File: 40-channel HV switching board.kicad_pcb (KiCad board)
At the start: 4 copper layers, 84 x 94 mm, 194 parts, among them IC1 ATMEGA328P-A, J1 TFM-125-02-X-DH, P1 CONN_01X06, P2 CONN_01X06, P3 CONN_01X01, P4 CONN_01X01, P5 CONN_01X01, P6 CONN_01X01, U1 74HC595A, U2 74HC595A, U3 74HC595A, U4 74HC595A, U5 74HC595A, U6 W25Q64FV, Y1 RESONATOR

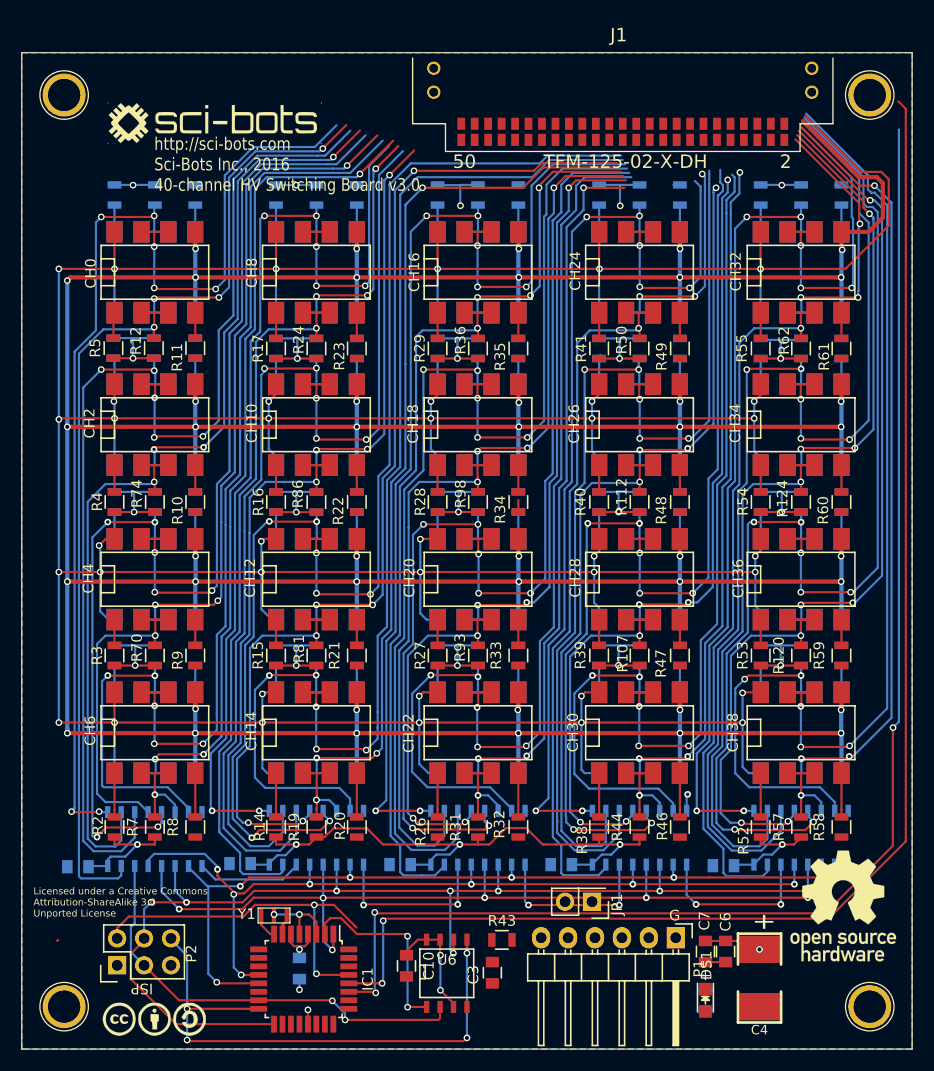
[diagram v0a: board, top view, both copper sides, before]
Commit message: Lots of fixes to prepare for EMC testing
* read output of shift registers
* fix flash chip connection
* replace jumpers with 0805 pads
* reduce length to 92mm
* filter i2c lines
* protect i2c lines
* add ferrites to SPI lines
* add chasis ground ring
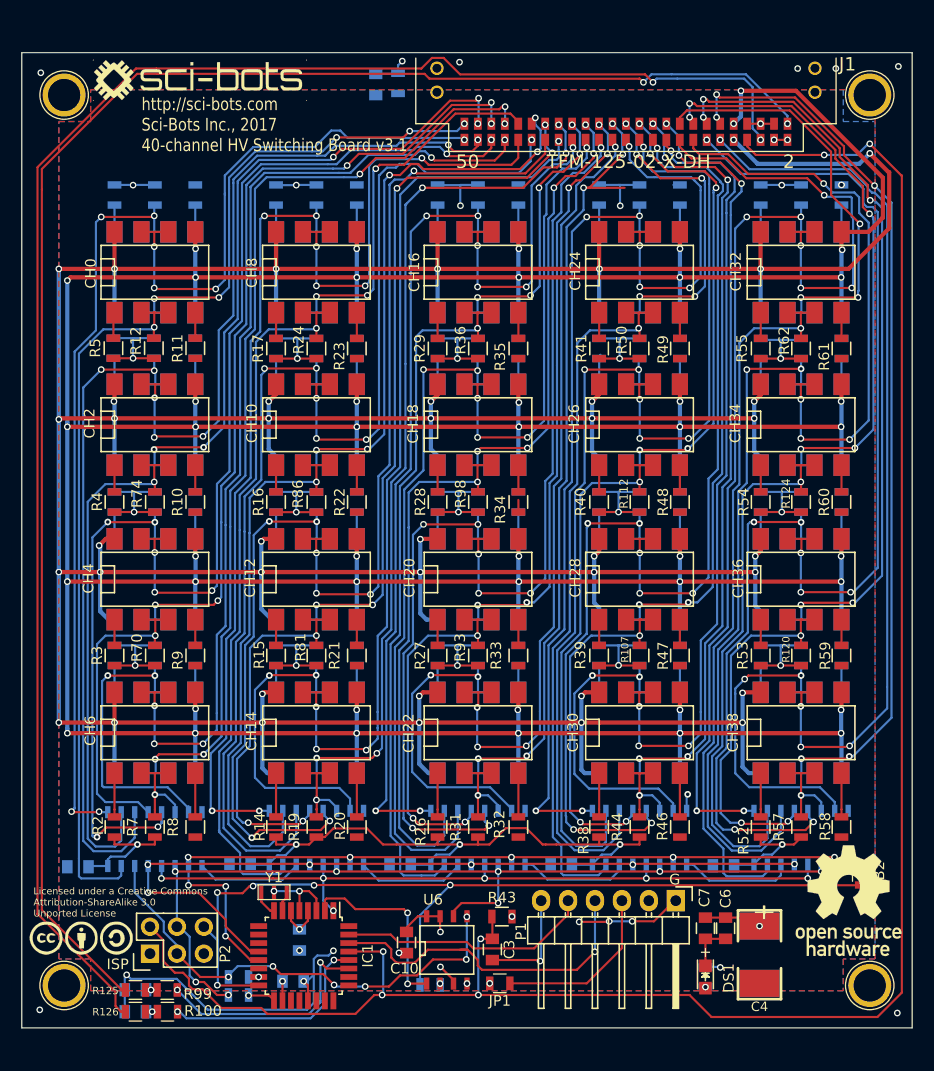
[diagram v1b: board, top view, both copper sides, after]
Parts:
- added C11: 0.1uF, Capacitors_SMD:C_0805, B.Cu at (49.6, 110.6)
- added C14: C, Capacitors_SMD:C_0805, B.Cu at (34.7, 111.4)
- added C15: C, Capacitors_SMD:C_0805, B.Cu at (34.7, 113.5)
- added C16: 0.1uF, Capacitors_SMD:C_0805, B.Cu at (57.4, 26.0)
- added FB1: FERRITE, Resistors_SMD:R_0805, B.Cu at (44.5, 110.2)
- added FB2: FERRITE, Resistors_SMD:R_0805, F.Cu at (103.2, 100.6)
- added FB3: FERRITE, Resistors_SMD:R_0805, B.Cu at (44.5, 111.9)
- added FB4: FERRITE, Resistors_SMD:R_0805, B.Cu at (62.5, 111.0)
- added FB5: FERRITE, Resistors_SMD:R_0805, B.Cu at (59.5, 25.9)
- added R100: R, Resistors_SMD:R_0805, F.Cu at (37.8, 113.5)
- added R125: R, Resistors_SMD:R_0805, F.Cu at (34.7, 111.4)
- added R126: R, Resistors_SMD:R_0805, F.Cu at (34.7, 113.5)
- added R99: R, Resistors_SMD:R_0805, F.Cu at (37.7, 111.4)
- JP1: footprint Pin_Headers:Pin_Header_Straight_2x01 -> Resistors_SMD:R_0805
- moved JP1 11.6 mm to (69.1, 110.8)
- moved G*** 10.3 mm to (29.6, 106.5)
- moved G*** 4.29 mm to (40.8, 25.6)
- moved P1 3.50 mm to (85.7, 103.0)
- moved P2 3.29 mm to (36.1, 108.0)
- moved C13 2.70 mm to (50.2, 106.7)
- moved C10 2.20 mm to (60.3, 107.0)
- moved C2 2.20 mm to (93.6, 108.1)
- moved C3 2.20 mm to (68.4, 107.6)
- moved C4 2.20 mm to (93.6, 108.1)
- moved C6 2.20 mm to (90.4, 105.6)
- moved C7 2.20 mm to (88.5, 105.6)
- moved DS1 2.20 mm to (88.5, 110.2)
- moved IC1 2.20 mm to (50.6, 108.2)
- moved R43 2.20 mm to (69.3, 104.5)
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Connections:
- IC1 pad 15: D11/MOSI -> Net-(FB1-Pad1)
- IC1 pad 17: D13/SCK -> Net-(FB3-Pad1)
- IC1 pad 27: A4/SDA -> Net-(IC1-Pad27)
- IC1 pad 28: A5/SCL -> Net-(IC1-Pad28)
- J1 pad 1: HVOUT0 -> A4/SDA
- J1 pad 10: HVOUT9 -> HVGND
- J1 pad 11: HVOUT10 -> HVOUT39
- J1 pad 12: HVOUT11 -> HVOUT38
- J1 pad 13: HVOUT12 -> HVOUT37
- J1 pad 14: HVOUT13 -> HVOUT36
- J1 pad 15: HVOUT14 -> HVOUT35
- J1 pad 16: HVOUT15 -> HVOUT34
- J1 pad 17: HVOUT16 -> HVOUT33
- J1 pad 18: HVOUT17 -> HVOUT32
- J1 pad 19: HVOUT18 -> HVOUT31
- J1 pad 2: HVOUT1 -> +3.3V
- J1 pad 20: HVOUT19 -> HVOUT30
- J1 pad 21: HVOUT20 -> HVOUT29
- J1 pad 22: HVOUT21 -> HVOUT28
- J1 pad 23: HVOUT22 -> HVOUT27
- J1 pad 24: HVOUT23 -> HVOUT26
- J1 pad 25: HVOUT24 -> HVOUT25
- J1 pad 26: HVOUT25 -> HVOUT24
- J1 pad 27: HVOUT26 -> HVOUT23
- J1 pad 28: HVOUT27 -> HVOUT22
- J1 pad 29: HVOUT28 -> HVOUT21
- J1 pad 3: HVOUT2 -> GND
- J1 pad 30: HVOUT29 -> HVOUT20
- J1 pad 31: HVOUT30 -> HVOUT19
- J1 pad 32: HVOUT31 -> HVOUT18
- J1 pad 33: HVOUT32 -> HVOUT17
- J1 pad 34: HVOUT33 -> HVOUT16
- J1 pad 35: HVOUT34 -> HVOUT15
- J1 pad 36: HVOUT35 -> HVOUT14
- J1 pad 37: HVOUT36 -> HVOUT13
- J1 pad 38: HVOUT37 -> HVOUT12
- J1 pad 39: HVOUT38 -> HVOUT11
- J1 pad 4: HVOUT3 -> +3.3V
- J1 pad 40: HVOUT39 -> HVOUT10
- J1 pad 41: HV -> HVOUT9
- J1 pad 42: HVGND -> HVOUT8
- J1 pad 43: GND -> HVOUT7
- J1 pad 44: RST -> HVOUT6
- J1 pad 45: GND -> HVOUT5
- J1 pad 46: A5/SCL -> HVOUT4
- J1 pad 47: GND -> HVOUT3
- J1 pad 48: +3.3V -> HVOUT2
- J1 pad 49: A4/SDA -> HVOUT1
- J1 pad 5: HVOUT4 -> GND
- J1 pad 50: +3.3V -> HVOUT0
- J1 pad 6: HVOUT5 -> A5/SCL
- J1 pad 7: HVOUT6 -> GND
- J1 pad 8: HVOUT7 -> RST
- J1 pad 9: HVOUT8 -> HV
- P3 pad 1: GND -> CHASIS_GND
- P4 pad 1: GND -> CHASIS_GND
- P5 pad 1: GND -> CHASIS_GND
- P6 pad 1: GND -> CHASIS_GND
- U6 pad 2: D11/MOSI -> Net-(FB4-Pad1)
- U6 pad 5: D12/MISO -> D11/MOSI
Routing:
- net RST: track 35.0 -> 189.2 mm, vias 2 -> 6
- net GND: track 17.2 -> 62.8 mm, vias 5 -> 14
- net D12/MISO: track 53.0 -> 86.4 mm, vias 4 -> 5
- net TX: track 0.00 -> 32.3 mm, vias 0 -> 1
- net CHASIS_GND: track 0.00 -> 31.3 mm, vias 0 -> 8
- net A5/SCL: track 131.6 -> 161.9 mm
- net A4/SDA: track 129.6 -> 158.2 mm, vias 3 -> 2
- net RX: track 0.00 -> 23.9 mm
- net Net-(IC1-Pad27): track 0.00 -> 21.6 mm, vias 0 -> 2
- net Net-(IC1-Pad28): track 0.00 -> 20.7 mm, vias 0 -> 2
- net D13/SCK: track 108.2 -> 88.1 mm
- net HVOUT11: track 38.9 -> 55.6 mm, vias 3 -> 5
- net +3.3V_USB: track 0.00 -> 16.4 mm
- net HVOUT3: track 48.8 -> 64.1 mm, vias 3 -> 5
- net HVOUT35: track 42.4 -> 57.2 mm, vias 3 -> 5
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- added copper zone on GND, net CHASIS_GND
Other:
- board size 84 x 94 mm -> 84 x 92 mm
- board text added: "http://sci-bots.com Sci-Bots Inc., 2017 40-channel HV Switching Board v3.1"
- board text removed: "http://sci-bots.com Sci-Bots Inc., 2016 40-channel HV Switching Board v3.0"

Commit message: Update part numbers for i2c filters
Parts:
- C14, C15: value C -> 150pF
- R100, R99: value R -> 51
- R125, R126: value R -> 150
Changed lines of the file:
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@@
       (effects (font (size 0.8 0.8) (thickness 0.1)) (justify mirror))
     )
-    (fp_text value C (at 0 -1.75) (layer B.Fab)
+    (fp_text value 150pF (at 0 -1.75) (layer B.Fab)
       (effects (font (size 1 1) (thickness 0.15)) (justify mirror))
     )
@@
       (effects (font (size 0.8 0.8) (thickness 0.1)) (justify mirror))
     )
-    (fp_text value C (at 0 -1.75) (layer B.Fab)
+    (fp_text value 150pF (at 0 -1.75) (layer B.Fab)
       (effects (font (size 1 1) (thickness 0.15)) (justify mirror))
     )
@@
       (effects (font (size 1 1) (thickness 0.15)))
     )
-    (fp_text value R (at 0 1.75) (layer F.Fab)
+    (fp_text value 51 (at 0 1.75) (layer F.Fab)
       (effects (font (size 1 1) (thickness 0.15)))
     )
@@
       (effects (font (size 1 1) (thickness 0.15)))
     )
-    (fp_text value R (at 0 1.75) (layer F.Fab)
+    (fp_text value 51 (at 0 1.75) (layer F.Fab)
       (effects (font (size 1 1) (thickness 0.15)))
     )
@@
       (effects (font (size 0.7 0.7) (thickness 0.1)))
     )
-    (fp_text value R (at 0 1.75) (layer F.Fab)
+    (fp_text value 150 (at 0 1.75) (layer F.Fab)
       (effects (font (size 1 1) (thickness 0.15)))
     )
@@
       (effects (font (size 0.7 0.7) (thickness 0.1)))
     )
-    (fp_text value R (at 0 1.75) (layer F.Fab)
-      (effects (font (size 1 1) (thickness 0.15)))
-    )
+    (fp_text value 150 (at 0 1.75) (layer F.Fab)
+      (effects (font (size 1 1) (thickness 0.15)))
+    )

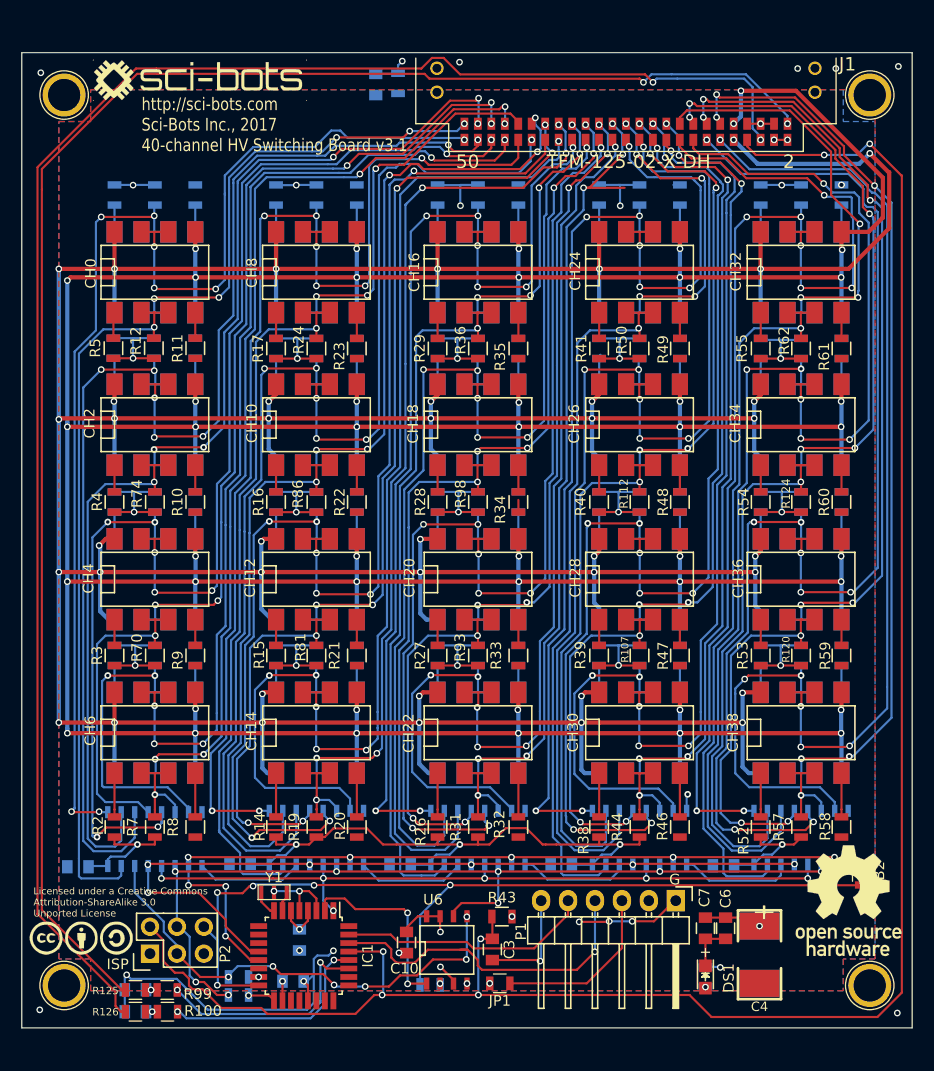
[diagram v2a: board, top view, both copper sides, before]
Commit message: Change resistor values use standard ref prefixes
* Fix #1 and #2
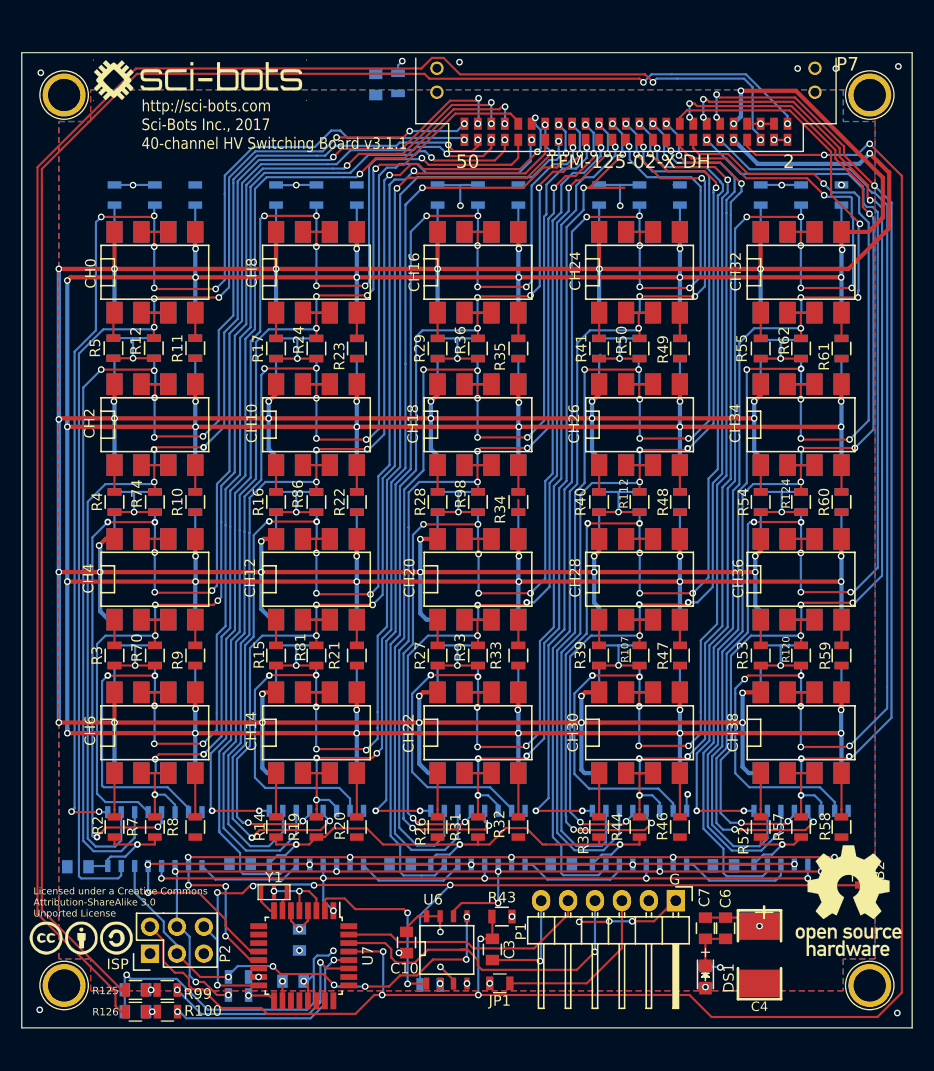
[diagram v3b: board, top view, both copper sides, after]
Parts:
- CH0, CH1, CH10, CH11, CH12, CH13, CH14, CH15, CH16, CH17, CH18, CH19, CH2, CH20, CH21, CH22, CH23, CH24, CH25, CH26, CH27, CH28, CH29, CH3, CH30, CH31, CH32, CH33, CH34, CH35, CH36, CH37, CH38, CH39, CH4, CH5, CH6, CH7, CH8, CH9: value AQW216 -> SSR-DPST
- R10, R102, R103, R104, R105, R108, R109, R11, R110, R111, R113, R115, R116, R117, R119, R121, R122, R123, R14, R15, R16, R17, R2, R20, R21, R22, R23, R26, R27, R28, R29, R3, R32, R33, R34, R35, R38, R39, R4, R40, R41, R46, R47, R48, R49, R5, R52, R53, R54, R55, R58, R59, R60, R61, R63, R65, R66, R67, R69, R71, R72, R73, R76, R77, R78, R79, R8, R82, R83, R84, R85, R88, R89, R9, R90, R91, R94, R95, R96, R97: value 300 -> 220
- U7: renamed from IC1; value ATMEGA328P-A -> ATMEGA328P-AU
- renumbered J1 to P7
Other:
- board text added: "http://sci-bots.com Sci-Bots Inc., 2017 40-channel HV Switching Board v3.1.1"
- board text removed: "http://sci-bots.com Sci-Bots Inc., 2017 40-channel HV Switching Board v3.1"

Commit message: Modify to use Sci-Bots library submodule
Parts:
- C2, C4: footprint WheelerLab:SM2917 -> Sci-Bots:SM2917
- G***: footprint WheelerLab:OSHW_logo_10mm -> Sci-Bots:OSHW_logo_10mm
- G***: footprint WheelerLab:CC_S_A_logo_10mm -> Sci-Bots:CC_S_A_logo_10mm
- P7: footprint WheelerLab:TFM-125-02-X-DH -> Sci-Bots:TFM-125-02-X-DH
- U1, U2, U3, U4, U5: footprint WheelerLab:SO16E -> Sci-Bots:SO16E
- Y1: footprint WheelerLab:CSTCE_G15C -> Sci-Bots:CSTCE_G15C
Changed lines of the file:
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@@
       (xy 10.0584 -1.9304) (xy 10.100851 -1.91244)) (layer F.SilkS) (width 0.01))
   )
-  (module WheelerLab:SM2917 (layer Back)
+  (module Sci-Bots:SM2917 (layer Back)
     (at 93.6 108.1 270)
     (fp_text reference C2 (at -3.5 -3.2 360) (layer B.SilkS)
@@
     )
   )
-  (module WheelerLab:SM2917 (layer Front)
+  (module Sci-Bots:SM2917 (layer Front)
     (at 93.6 108.1 270)
     (fp_text reference C4 (at 4.9 0 360) (layer F.SilkS)
@@
     )
   )
-  (module WheelerLab:SO16E (layer Back)
+  (module Sci-Bots:SO16E (layer Back)
     (at 36.56125 97.19175)
     (descr "Module CMS SOJ 16 pins etroit")
@@
     )
   )
-  (module WheelerLab:SO16E (layer Back)
+  (module Sci-Bots:SO16E (layer Back)
     (at 51.80125 97.06475)
     (descr "Module CMS SOJ 16 pins etroit")
@@
     )
   )
-  (module WheelerLab:SO16E (layer Back)
+  (module Sci-Bots:SO16E (layer Back)
     (at 67.04125 97.06475)
     (descr "Module CMS SOJ 16 pins etroit")
@@
     )
   )
-  (module WheelerLab:SO16E (layer Back)
+  (module Sci-Bots:SO16E (layer Back)
     (at 82.28125 97.06475)
     (descr "Module CMS SOJ 16 pins etroit")
@@
     )
   )
-  (module WheelerLab:SO16E (layer Back)
+  (module Sci-Bots:SO16E (layer Back)
     (at 97.52125 97.06475)
     (descr "Module CMS SOJ 16 pins etroit")
@@
     )
   )
-  (module WheelerLab:OSHW_logo_10mm (layer Front)
+  (module Sci-Bots:OSHW_logo_10mm (layer Front)
     (at 102 103)
     (fp_text reference G*** (at 0 0) (layer F.SilkS) hide
@@
       (xy -0.522042 -5.212843) (xy -0.507346 -5.226922) (xy 0.507808 -5.226922) (xy 0.522657 -5.211981)) (layer F.SilkS) (width 0.01))
   )
-  (module WheelerLab:CC_S_A_logo_10mm (layer Front)
+  (module Sci-Bots:CC_S_A_logo_10mm (layer Front)
     (at 29.6 106.5)
     (fp_text reference G*** (at 0 0) (layer F.SilkS) hide
@@
     )
   )
-  (module WheelerLab:CSTCE_G15C (layer Front)
+  (module Sci-Bots:CSTCE_G15C (layer Front)
     (at 47.8 102.2 180)
     (fp_text reference Y1 (at 0 1.4 180) (layer F.SilkS)
@@
     )
   )
-  (module WheelerLab:TFM-125-02-X-DH (layer Front)
+  (module Sci-Bots:TFM-125-02-X-DH (layer Front)
     (at 81 23)
     (descr "0.050\" DOUBLE HORIZONTAL TERMINAL STRIP.")
